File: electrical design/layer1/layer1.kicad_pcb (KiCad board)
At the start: 2 copper layers, 178 x 168.1 mm, 215 parts, among them J1 XT60-F, J10 Conn_01x02_Pin, J2 Conn_01x01_Socket, J4 XT30PW-F, J5 Conn_01x01_Socket, J6 Conn_01x01_Socket, J7 Conn_01x01_Socket, J8 Conn_01x01_Socket, J9 Conn_01x02_Pin, Q1 MOSFET-NCH-FQP30N06L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

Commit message: update layer 1 design files
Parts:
- added J11: Conn_01x01_Socket, Connector_Wire:SolderWirePad_1x01_SMD_1x2mm, F.Cu at (39.0, 127.2)
- added J12: Conn_01x01_Socket, Connector_Wire:SolderWire-0.5sqmm_1x01_D0.9mm_OD2.1mm, F.Cu at (88.5, 122.2)
- added J13: Conn_01x05_Pin, Connector_JST:JST_SH_BM05B-SRSS-TB_1x05-1MP_P1.00mm_Vertical, F.Cu at (179.2, 119.6)
- added J14: Conn_01x02_Pin, Connector_JST:JST_SH_BM02B-SRSS-TB_1x02-1MP_P1.00mm_Vertical, F.Cu at (75.0, 105.0)
- added J3: Conn_01x01_Socket, Connector_Wire:SolderWirePad_1x01_SMD_5x10mm, F.Cu at (39.0, 105.0)
- added TP1: TestPoint_2Pole, TestPoint:TestPoint_2Pads_Pitch2.54mm_Drill0.8mm, B.Cu at (105.5, 186.0)
- added TP2: TestPoint_2Pole, TestPoint:TestPoint_2Pads_Pitch2.54mm_Drill0.8mm, B.Cu at (68.5, 174.0)
- added TP3: TestPoint_2Pole, TestPoint:TestPoint_2Pads_Pitch2.54mm_Drill0.8mm, B.Cu at (33.0, 92.0)
- added TP4: TestPoint_2Pole, TestPoint:TestPoint_2Pads_Pitch2.54mm_Drill0.8mm, B.Cu at (33.0, 113.0)
- BUCK1: value +5V -> VCCQ; footprint Connector_PinHeader_2.54mm:PinHeader_1x03_P2.54mm_Vertical -> Connector_PinSocket_2.54mm:PinSocket_1x03_P2.54mm_Horizontal
- BUCK2: footprint Connector_PinHeader_2.54mm:PinHeader_1x03_P2.54mm_Vertical -> Connector_PinSocket_2.54mm:PinSocket_1x03_P2.54mm_Horizontal
- J1: value XT60-F -> XT30-F
- J2: footprint Connector_Wire:SolderWire-0.75sqmm_1x01_D1.25mm_OD2.3mm -> Connector_Wire:SolderWirePad_1x01_SMD_1x2mm
- moved SW1 139.8 mm to (39.0, 123.0)
- moved J2 45.6 mm to (114.8, 135.6), turned to 90 degrees
- moved BUCK1 12.5 mm to (37.8, 92.0)
- moved BUCK2 12.5 mm to (37.8, 113.0)
- moved R39 1.25 mm to (124.8, 100.0)
- moved R37 1.17 mm to (85.3, 110.0)
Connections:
- net Net-(SW1A-B) renamed /LED
- BUCK1 pad 1: +5V -> VCCQ
- U3 pad 10: unconnected-(U3-PA5_A9_D9_MISO-Pad10) -> /BALL
- U3 pad 13: GND -> GNDD
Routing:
- net +5V: track 188.0 -> 8.00 mm, vias 2 -> 0
- net +3V3: track 145.9 -> 280.5 mm
- net GNDD: track 0.00 -> 120.3 mm, vias 0 -> 2
- net +12V: track 170.7 -> 58.8 mm
- net /BALL: track 0.00 -> 99.0 mm, vias 0 -> 5
- net /SOLENOIDON: track 6.40 -> 96.3 mm, vias 0 -> 4
- net VCCQ: track 312.3 -> 373.1 mm
- net GND: track 280.6 -> 228.7 mm, vias 103 -> 101
- net GNDA: track 92.4 -> 139.3 mm, vias 0 -> 1
- net +48V: track 0.85 -> 36.7 mm
- net /TX: track 0.00 -> 29.0 mm, vias 0 -> 3
- net /RX: track 0.00 -> 10.1 mm, vias 0 -> 1
- net /LED: track 60.3 -> 58.3 mm, vias 26 -> 16
- net Net-(U2-~{E}): track 8.29 -> 7.04 mm
- net Net-(U1-~{E}): track 8.13 -> 6.96 mm
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- added copper zone on B.Cu, net +3V3
- removed copper zone on F.Cu, net +3V3
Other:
- board text added: "+12V"
- board text added: "+3V3"
- board text added: "+48V"
- board text added: "VCCQ"
- board text added: "copyright © 2023. all rights reserved."
- board text added: "designed and assembled in singapore. made in china."
- board text removed: "12V"
- board text removed: "48V"

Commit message: update pcbs and mech drawings
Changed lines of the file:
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@@
         (effects (font (size 0.6096 0.6096) (thickness 0.127)))
     )
-    (fp_text value "SW_DPDT_x2" (at 2.921 0) (layer "F.SilkS")
+    (fp_text value "SW_DPDT_x2" (at 2.921 0) (layer "F.Fab")
         (effects (font (size 0.6096 0.6096) (thickness 0.127)))
     )

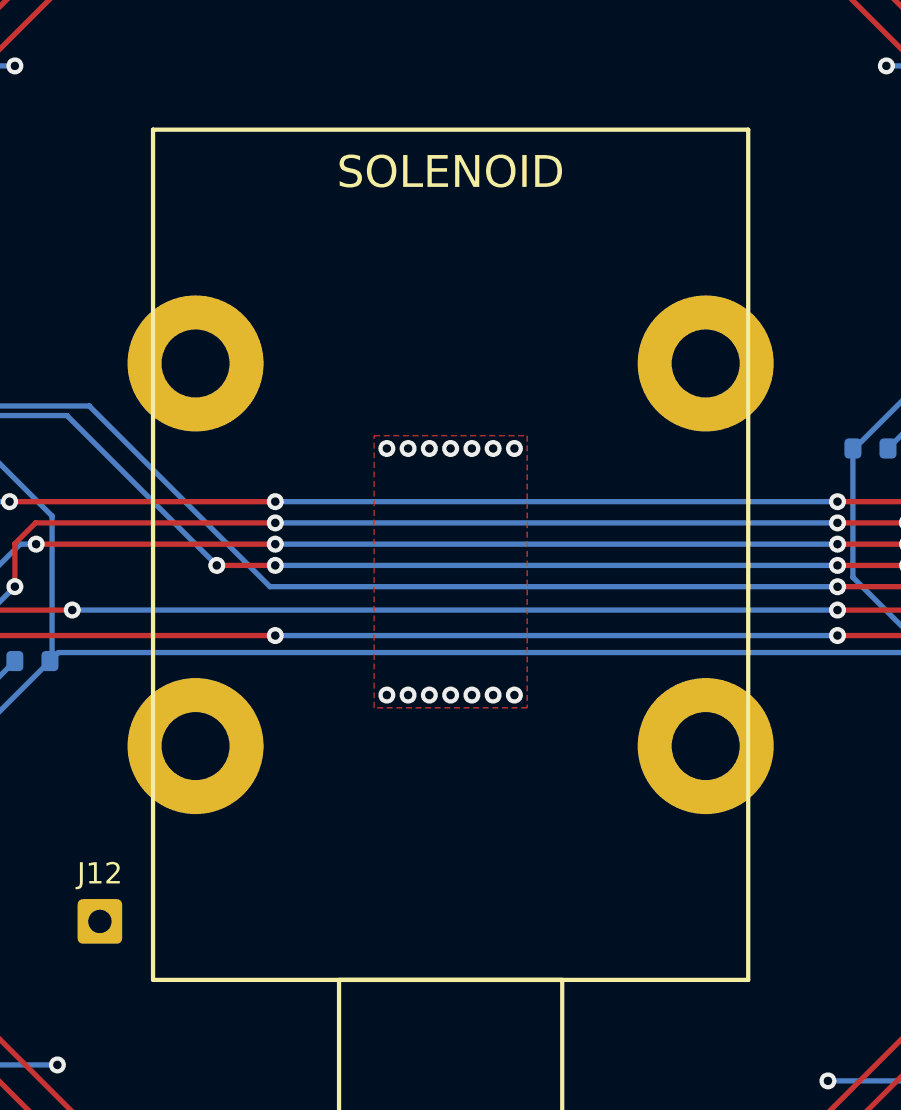
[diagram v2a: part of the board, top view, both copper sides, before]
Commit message: update pcbs for dual camera design
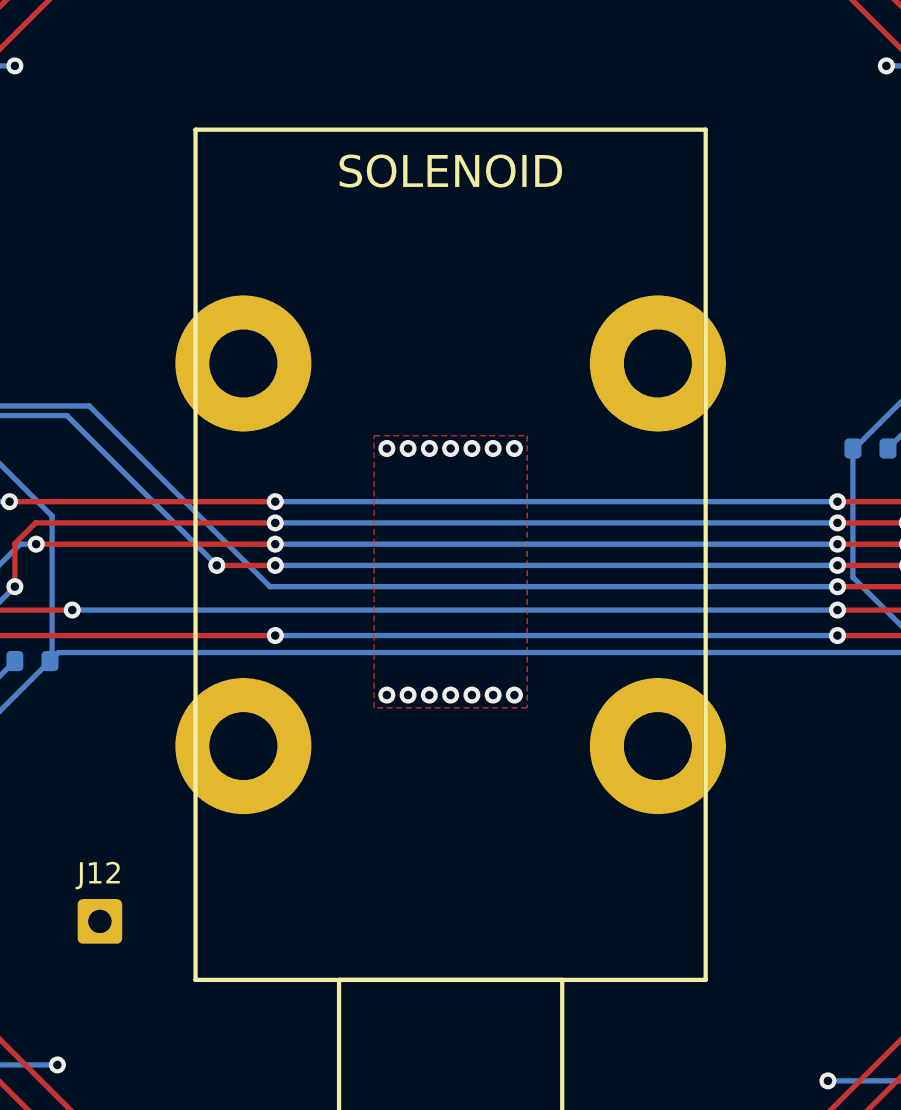
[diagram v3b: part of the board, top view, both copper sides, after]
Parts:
- moved H12 2.25 mm to (114.8, 114.0)
- moved H17 2.25 mm to (95.2, 114.0)
- moved H7 2.25 mm to (114.8, 96.0)
- moved H8 2.25 mm to (95.2, 96.0)
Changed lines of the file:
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@@
   )
   (footprint "MountingHole:MountingHole_3.2mm_M3_Pad" (layer "F.Cu")
-    (at 117 114)
+    (at 114.75 114)
     (descr "Mounting Hole 3.2mm, M3")
     (tags "mounting hole 3.2mm m3")
@@
   )
   (footprint "MountingHole:MountingHole_3.2mm_M3_Pad" (layer "F.Cu")
-    (at 93 96)
+    (at 95.25 96)
     (descr "Mounting Hole 3.2mm, M3")
     (tags "mounting hole 3.2mm m3")
@@
   )
   (footprint "MountingHole:MountingHole_3.2mm_M3_Pad" (layer "F.Cu")
-    (at 93 114)
+    (at 95.25 114)
     (descr "Mounting Hole 3.2mm, M3")
     (tags "mounting hole 3.2mm m3")
@@
   )
   (footprint "MountingHole:MountingHole_3.2mm_M3_Pad" (layer "F.Cu")
-    (at 117 96)
+    (at 114.75 96)
     (descr "Mounting Hole 3.2mm, M3")
     (tags "mounting hole 3.2mm m3")
@@
   (gr_rect (start 99.75 125) (end 110.25 148)
     (stroke (width 0.2) (type default)) (fill none) (layer "F.SilkS"))
-  (gr_rect locked (start 91 85) (end 119 125)
+  (gr_rect locked (start 93 85) (end 117 125)
     (stroke (width 0.2) (type solid)) (fill none) (layer "F.SilkS"))
   (gr_rect (start 80.5 153.8) (end 129.5 177.2)

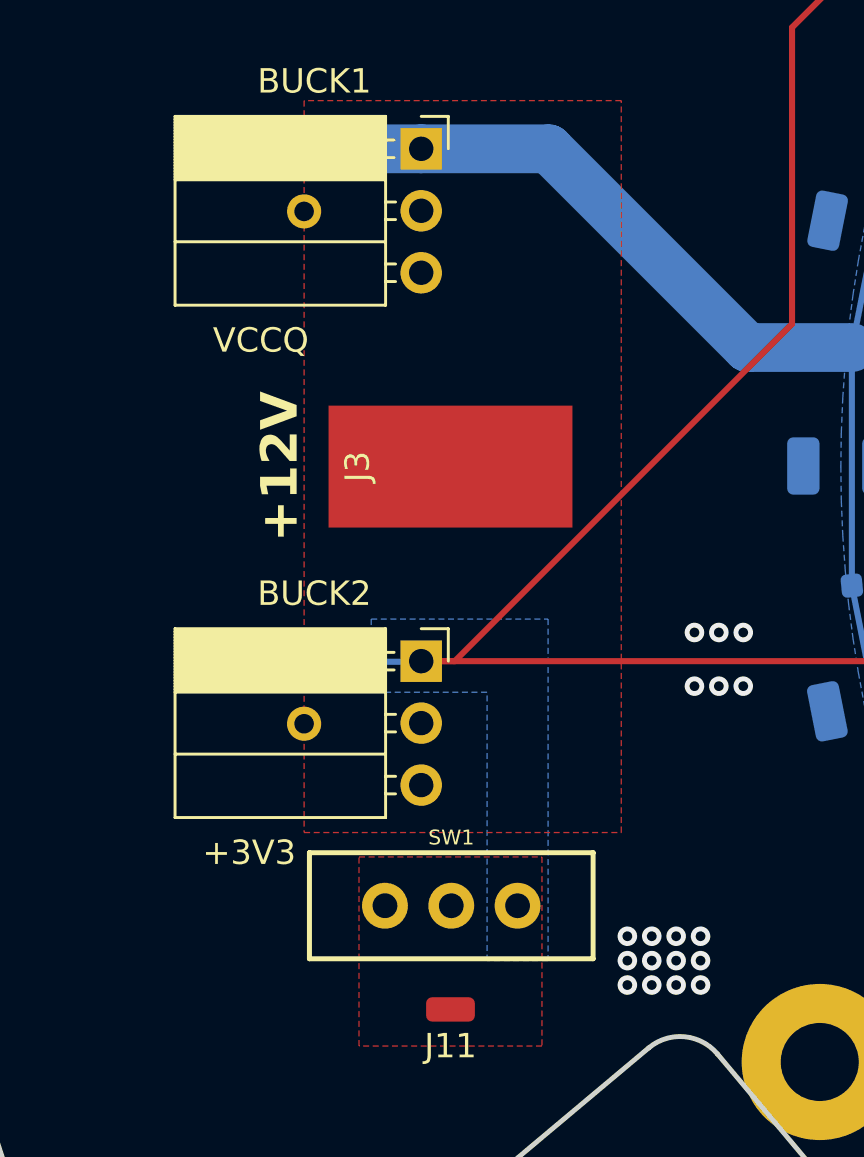
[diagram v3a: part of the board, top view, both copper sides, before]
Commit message: add fb between vccq and 3v3
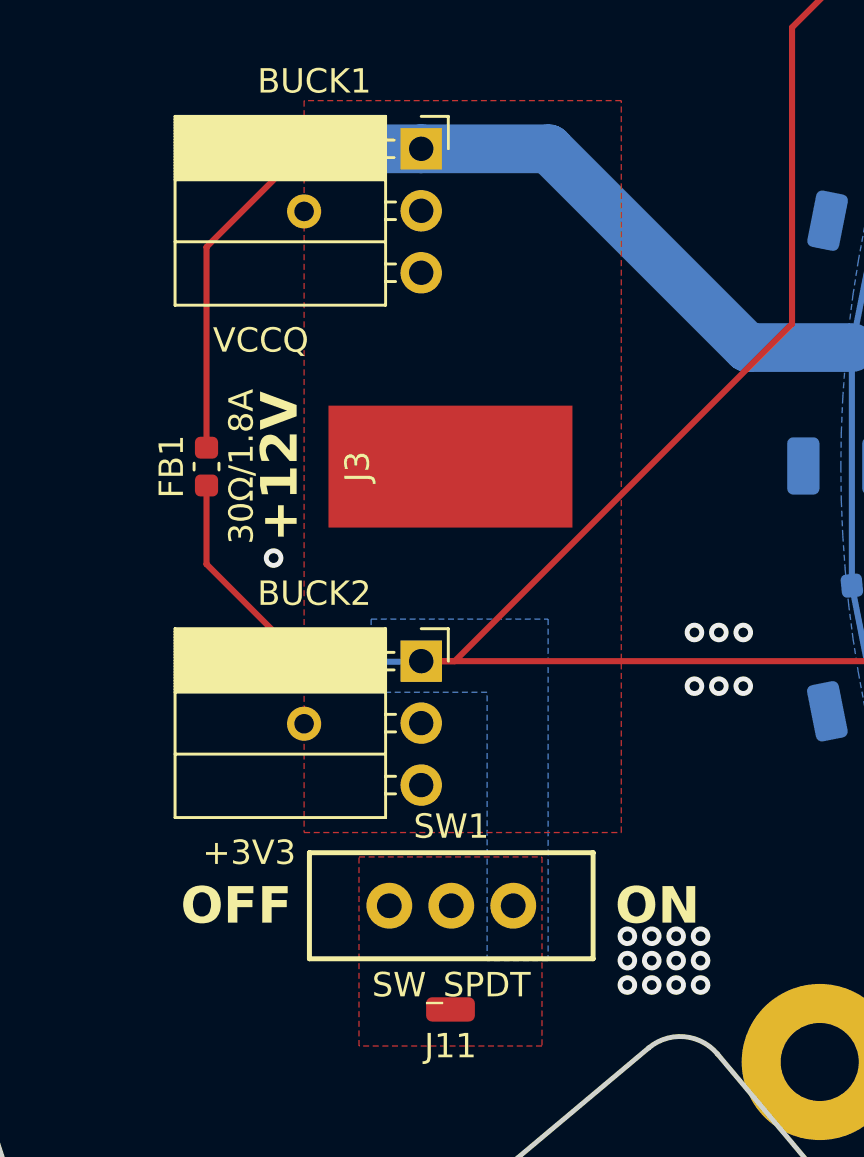
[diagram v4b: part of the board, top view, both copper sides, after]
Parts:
- added FB1: 30Ω/1.8A, Capacitor_SMD:C_0603_1608Metric, F.Cu at (29.0, 105.0)
- SW1: value SW_DPDT_x2 -> SW_SPDT; footprint Switches:SWITCH_SPDT_PTH_11.6X4.0MM_LOCK -> Switches:SWITCH_SPDT_PTH_11.6X4.0MM
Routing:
- net VCCQ: track 373.1 -> 387.0 mm
- net +3V3: track 280.5 -> 289.4 mm
- net GND: vias 101 -> 102
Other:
- board text added: "OFF"
- board text added: "ON"

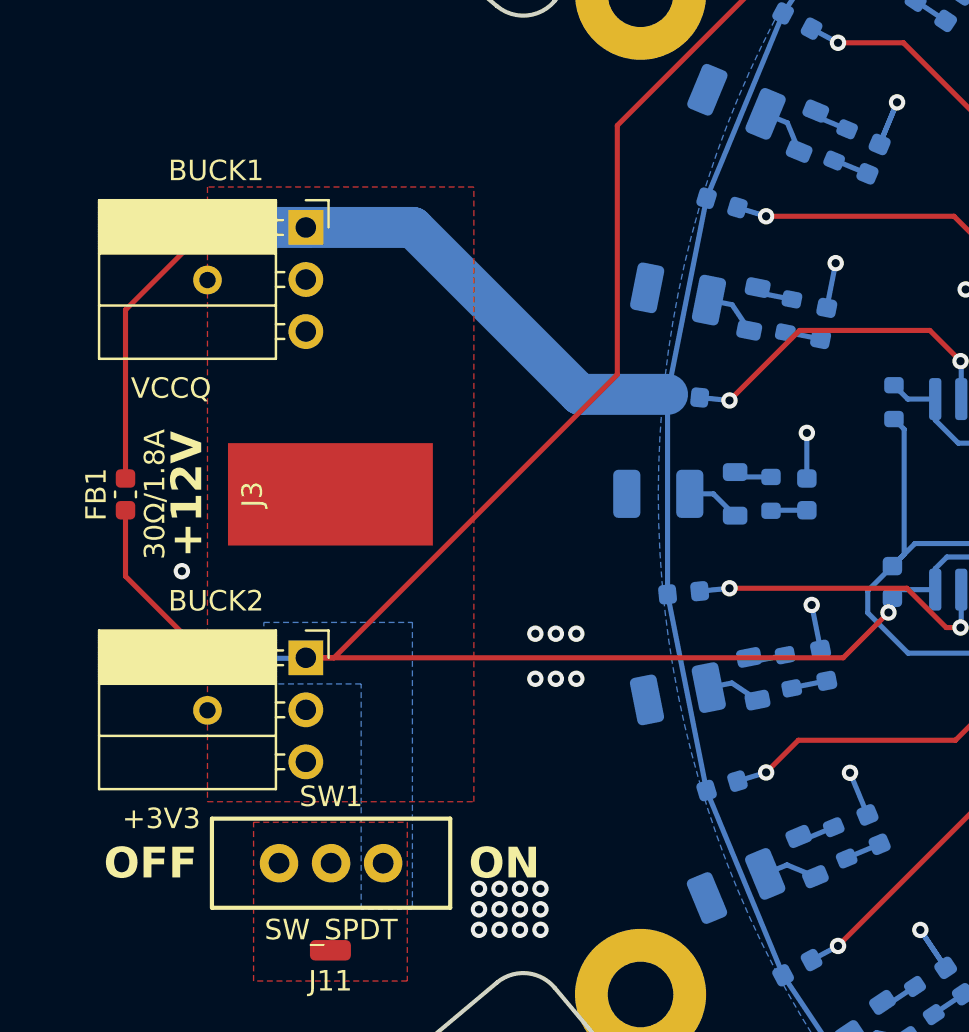
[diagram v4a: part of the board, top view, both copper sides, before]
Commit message: amend buck conv pinouts on l1 and l3
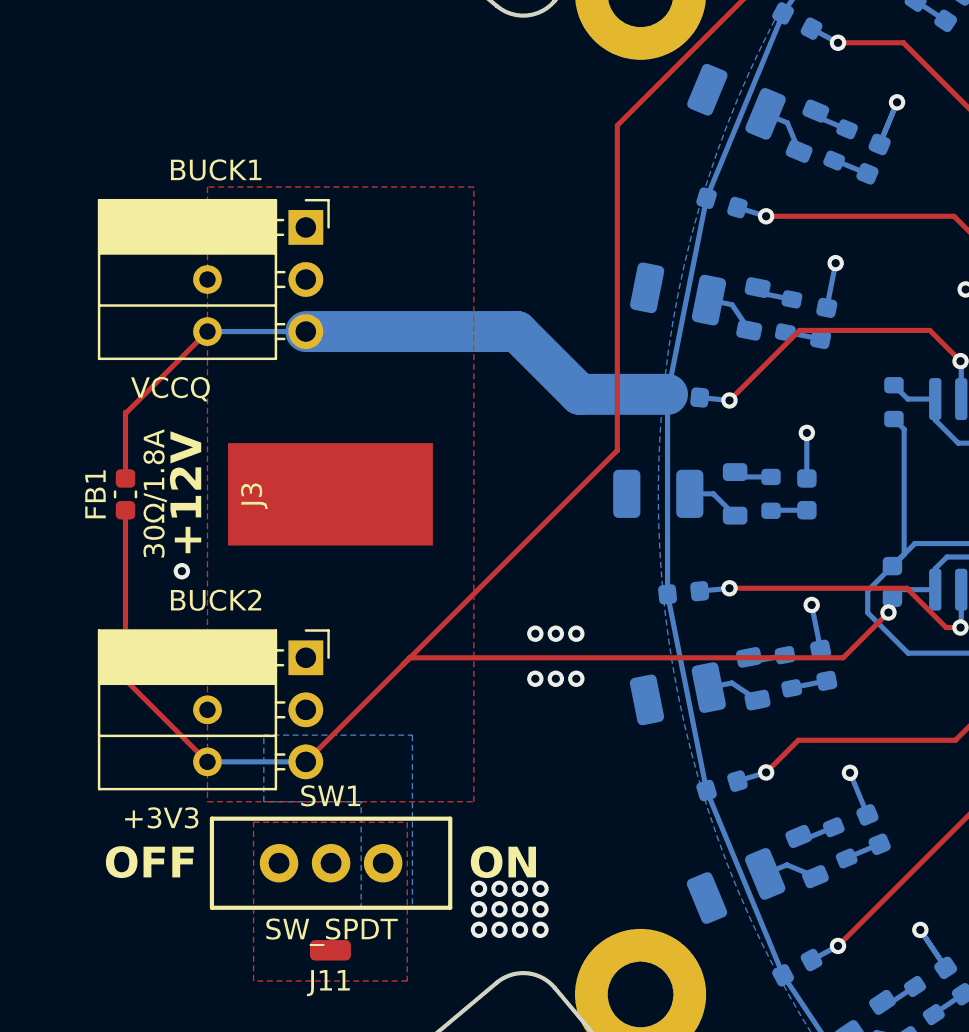
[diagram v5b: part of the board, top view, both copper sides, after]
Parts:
- moved TP3 5.06 mm to (33.0, 97.1), turned to 90 degrees
- moved TP4 5.06 mm to (33.0, 118.1), turned to 90 degrees
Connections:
- BUCK1 pad 1: VCCQ -> +12V
- BUCK1 pad 3: +12V -> VCCQ
- BUCK2 pad 1: +3V3 -> +12V
- BUCK2 pad 3: +12V -> +3V3
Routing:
- net VCCQ: track 387.0 -> 379.8 mm
- net +3V3: track 289.4 -> 294.1 mm
